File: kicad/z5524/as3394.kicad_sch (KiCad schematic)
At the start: 35 parts, among them U11 DG442DY-T1-E3, U14 TL074, U15 AS3394

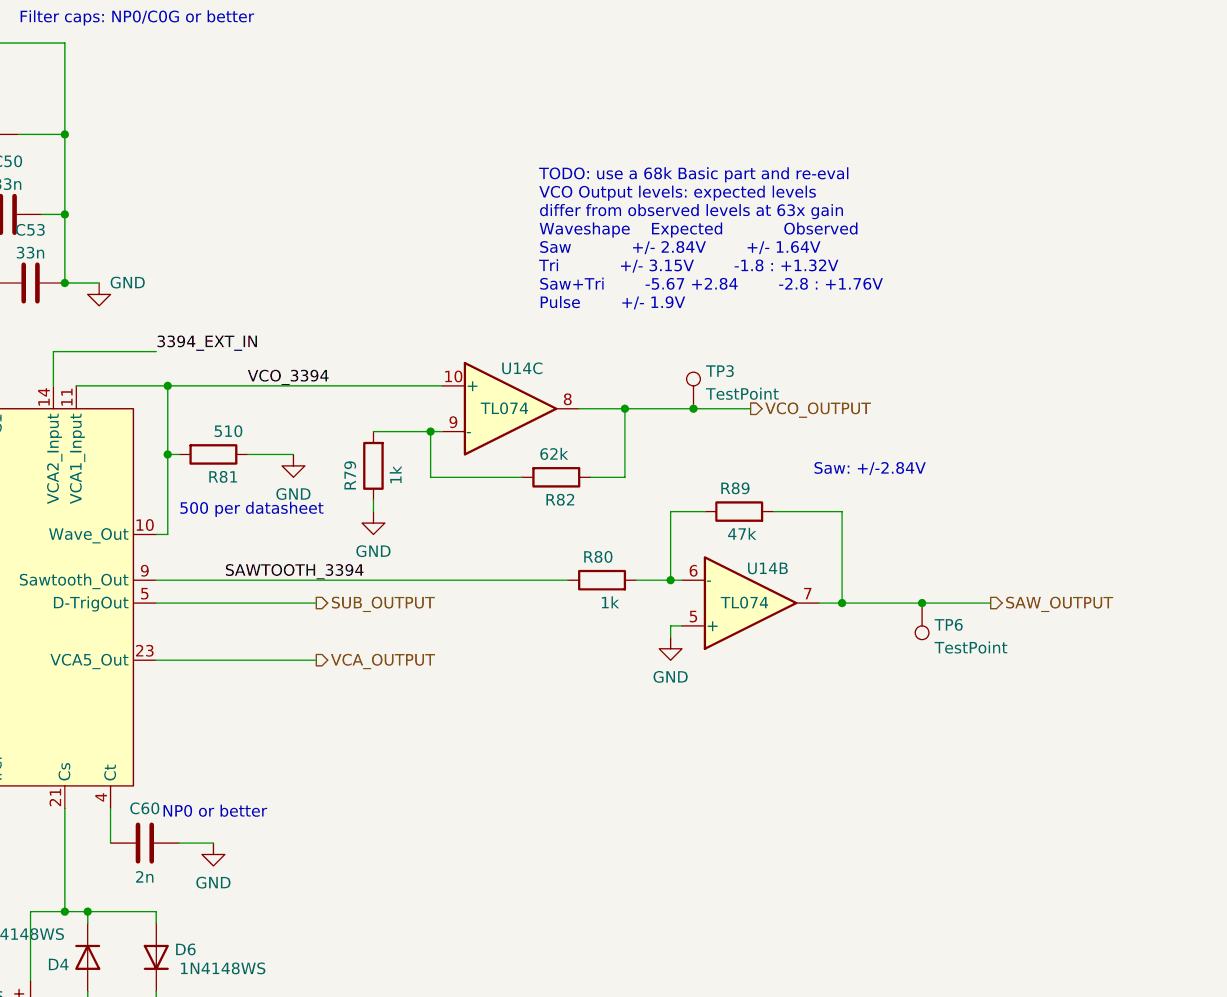
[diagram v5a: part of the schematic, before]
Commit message: increase FM depth on ssi2130
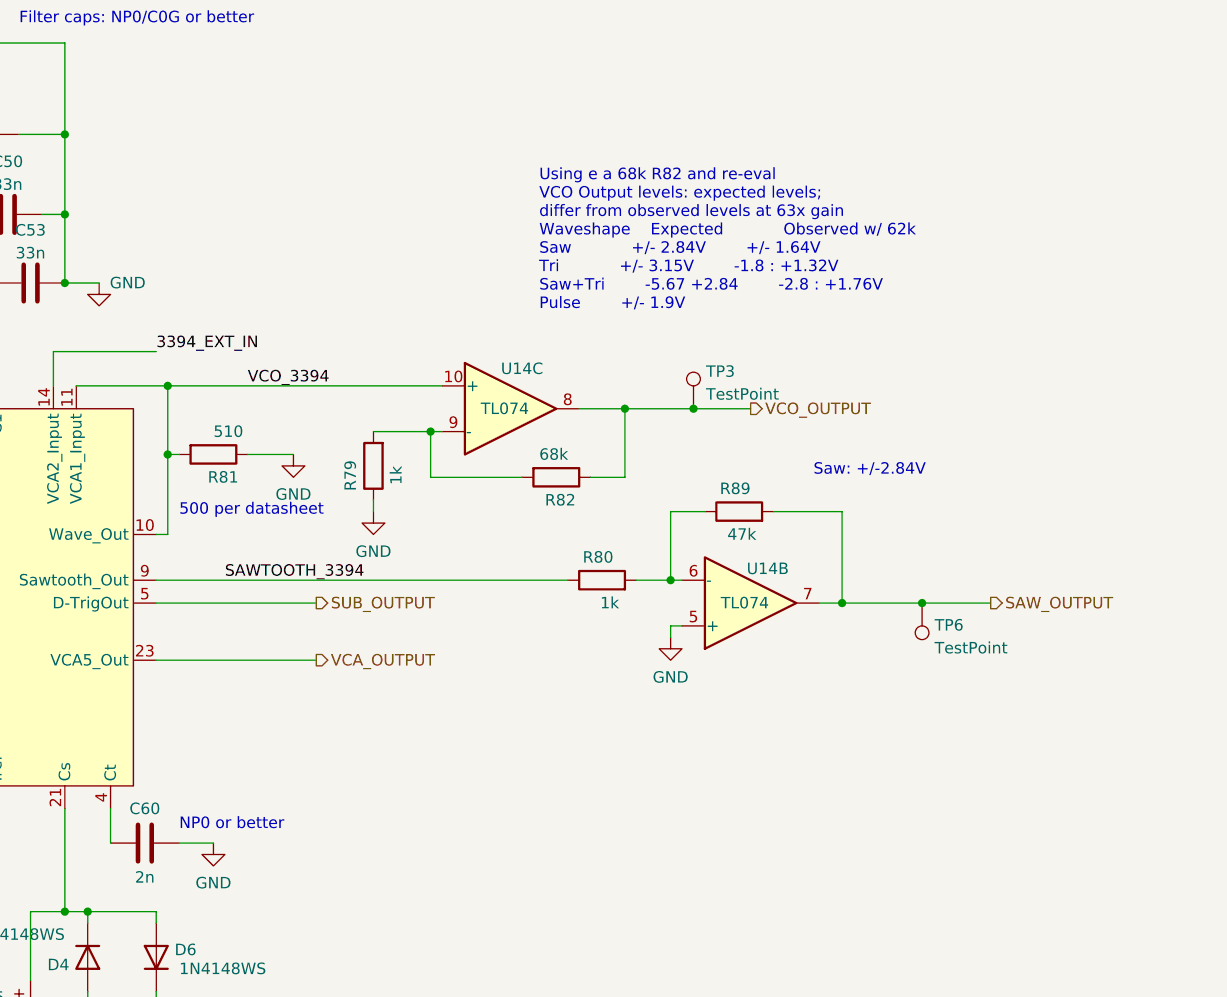
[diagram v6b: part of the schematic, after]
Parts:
- R82: value 62k -> 68k; LCSC C23221 -> C23231
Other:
- note added: "Using e a 68k R82 and re-eval VCO Output levels: expected levels; differ from observed levels at 63x gain Waveshape Expected Observed w/ 62k Saw +/- 2.84V +/- 1.64V Tri +/- 3.15V -1.8 : +1.32V Saw+Tri -5.67 +2.84 -2.8 : +1.76V Pulse +/- 1.9V"
- note removed: "TODO: use a 68k Basic part and re-eval VCO Output levels: expected levels differ from observed levels at 63x gain Waveshape Expected Observed Saw +/- 2.84V +/- 1.64V Tri +/- 3.15V -1.8 : +1.32V Saw+Tri -5.67 +2.84 -2.8 : +1.76V Pulse +/- 1.9V"
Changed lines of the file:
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@@
     (effects (font (size 1.27 1.27)) (justify left bottom))
   )
-  (text "NP0 or better" (at 159.385 151.13 0)
+  (text "NP0 or better" (at 161.29 152.4 0)
     (effects (font (size 1.27 1.27)) (justify left bottom))
   )
@@
     (effects (font (size 1.27 1.27)) (justify left bottom))
   )
-  (text "TODO: use a 68k Basic part and re-eval\nVCO Output levels: expected levels\ndiffer from observed levels at 63x gain\nWaveshape	Expected			Observed\nSaw			+/- 2.84V		+/- 1.64V\nTri			+/- 3.15V		-1.8 : +1.32V\nSaw+Tri		-5.67 +2.84		-2.8 : +1.76V\nPulse		+/- 1.9V			"
+  (text "Using e a 68k R82 and re-eval\nVCO Output levels: expected levels;\ndiffer from observed levels at 63x gain\nWaveshape	Expected			Observed w/ 62k\nSaw			+/- 2.84V		+/- 1.64V\nTri			+/- 3.15V		-1.8 : +1.32V\nSaw+Tri		-5.67 +2.84		-2.8 : +1.76V\nPulse		+/- 1.9V			"
     (at 201.295 94.615 0)
     (effects (font (size 1.27 1.27)) (justify left bottom))
@@
       (effects (font (size 1.27 1.27)) (justify left))
     )
-    (property "Value" "62k" (at 201.295 110.49 90)
+    (property "Value" "68k" (at 201.295 110.49 90)
       (effects (font (size 1.27 1.27)) (justify left))
     )
@@
       (effects (font (size 1.27 1.27)) hide)
     )
-    (property "LCSC" "C23221" (at 203.2 113.03 0)
-      (effects (font (size 1.27 1.27)) hide)
-    )
+    (property "LCSC" "C23231" (at 203.2 113.03 0)
+      (effects (font (size 1.27 1.27)) hide)
+    )

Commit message: z5524 v0.4 RTM
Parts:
- R54: LCSC (none) -> C4184
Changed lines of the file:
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@@
       (effects (font (size 1.27 1.27)) hide)
     )
-    (property "LCSC" "" (at 318.77 71.12 0)
+    (property "LCSC" "C4184" (at 318.77 71.12 0)
       (effects (font (size 1.27 1.27)) hide)
     )

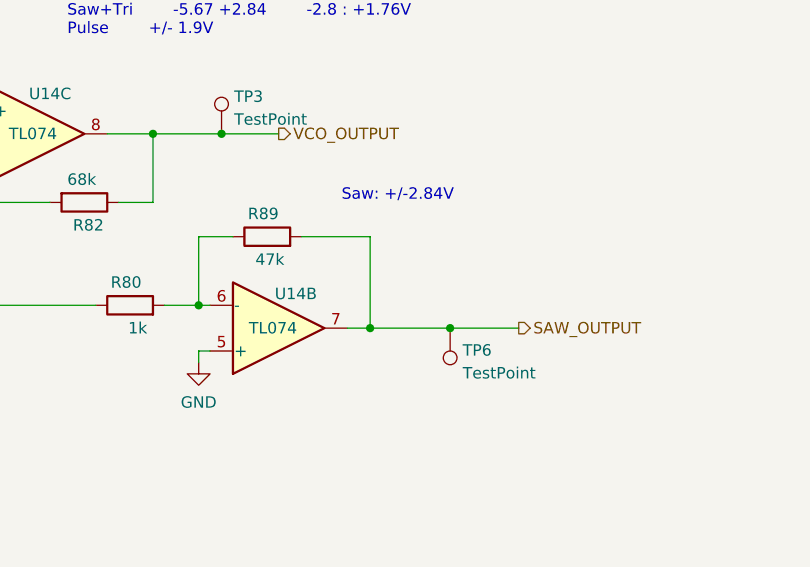
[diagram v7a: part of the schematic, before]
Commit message: updated to v0.5 of z5524
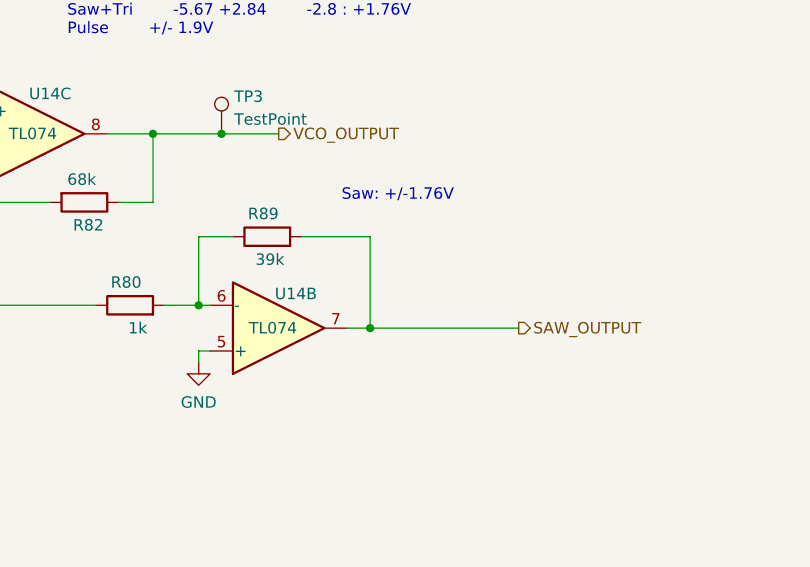
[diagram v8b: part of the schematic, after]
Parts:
- removed TP6: TestPoint, TestPoint:TestPoint_Pad_1.5x1.5mm, symbol Connector:TestPoint
- R89: value 47k -> 39k; LCSC C25819 -> C23153
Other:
- note added: "Saw: +/-1.76V"
- note removed: "Saw: +/-2.84V"
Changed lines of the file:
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@@
   (junction (at 72.39 34.29) (diameter 0) (color 0 0 0 0)
   )
-  (junction (at 243.84 127) (diameter 0) (color 0 0 0 0)
-  )
   (junction (at 388.62 54.61) (diameter 0) (color 0 0 0 0)
   )
@@
     (stroke (width 0) (type default))
   )
-  (wire (pts (xy 243.84 127) (xy 251.46 127))
+  (wire (pts (xy 234.95 127) (xy 251.46 127))
     (stroke (width 0) (type default))
   )
@@
   )
   (wire (pts (xy 144.78 184.15) (xy 151.13 184.15))
-    (stroke (width 0) (type default))
-  )
-  (wire (pts (xy 234.95 127) (xy 243.84 127))
     (stroke (width 0) (type default))
   )
@@
     (effects (font (size 1.27 1.27)) (justify left bottom))
   )
-  (text "Saw: +/-2.84V" (at 231.775 113.03 0)
+  (text "Saw: +/-1.76V" (at 231.775 113.03 0)
     (effects (font (size 1.27 1.27)) (justify left bottom))
   )
@@
     )
   )
-  (symbol (lib_id "Connector:TestPoint") (at 243.84 127 180) (unit 1)
-    (in_bom yes) (on_board yes) (dnp no) (fields_autoplaced)
-    (property "Reference" "TP6" (at 245.237 129.4673 0)
-      (effects (font (size 1.27 1.27)) (justify right))
-    )
-    (property "Value" "TestPoint" (at 245.237 132.0042 0)
-      (effects (font (size 1.27 1.27)) (justify right))
-    )
-    (property "Footprint" "TestPoint:TestPoint_Pad_1.5x1.5mm" (at 238.76 127 0)
-      (effects (font (size 1.27 1.27)) hide)
-    )
-    (property "Datasheet" "~" (at 238.76 127 0)
-      (effects (font (size 1.27 1.27)) hide)
-    )
-    (pin "1")
-    (instances
-      (project "z5524"
-        (path "/7079bdb0-a00e-4bac-b257-cbcf2c91bbd6/998834c5-8208-4d7e-a084-854ca45521ff"
-          (reference "TP6") (unit 1)
-        )
-      )
-    )
-  )
   (symbol (lib_id "Amplifier_Operational:TL074") (at 198.12 105.41 0) (unit 3)
     (in_bom yes) (on_board yes) (dnp no)
@@
       (effects (font (size 1.27 1.27)) (justify left))
     )
-    (property "Value" "47k" (at 225.425 119.38 90)
+    (property "Value" "39k" (at 225.425 119.38 90)
       (effects (font (size 1.27 1.27)) (justify left))
     )
@@
       (effects (font (size 1.27 1.27)) hide)
     )
-    (property "LCSC" "C25819" (at 223.52 116.84 90)
-      (effects (font (size 1.27 1.27)) hide)
-    )
+    (property "LCSC" "C23153" (at 223.52 116.84 90)
+      (effects (font (size 1.27 1.27)) hide)
+    )
